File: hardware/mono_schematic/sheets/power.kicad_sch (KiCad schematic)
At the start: 37 parts

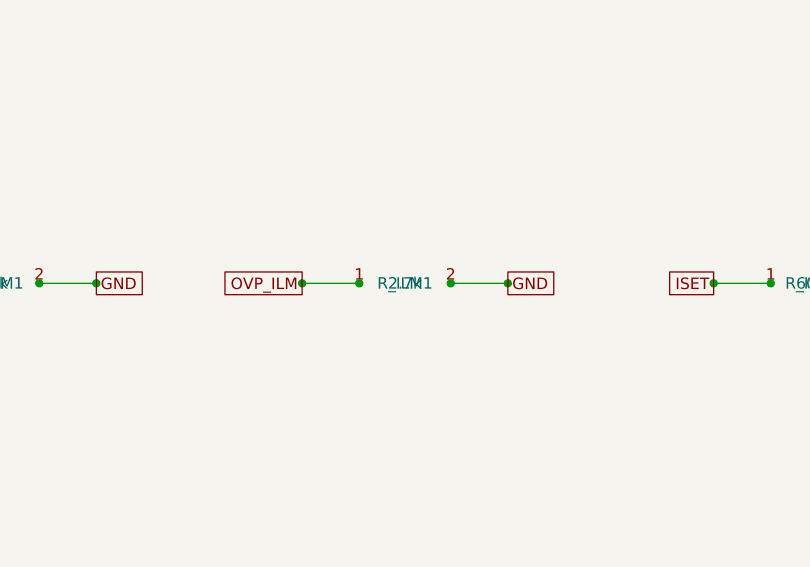
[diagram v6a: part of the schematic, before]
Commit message: mono_electronics v13c: R_ILM1 2.7k->1.6k (C4908; TPS2595 Eq.4 ILIM=2000/R+0.04 = 1.29 A, 1.19-1.39 A); U_OVP1 F GND pour 21.5 mm2 + 2 thermal vias; gates clean (DRC 0/0/0, ERC 0, 0 diffs, прозвонка 243/243); BOM/fab regen; abs-max review updated
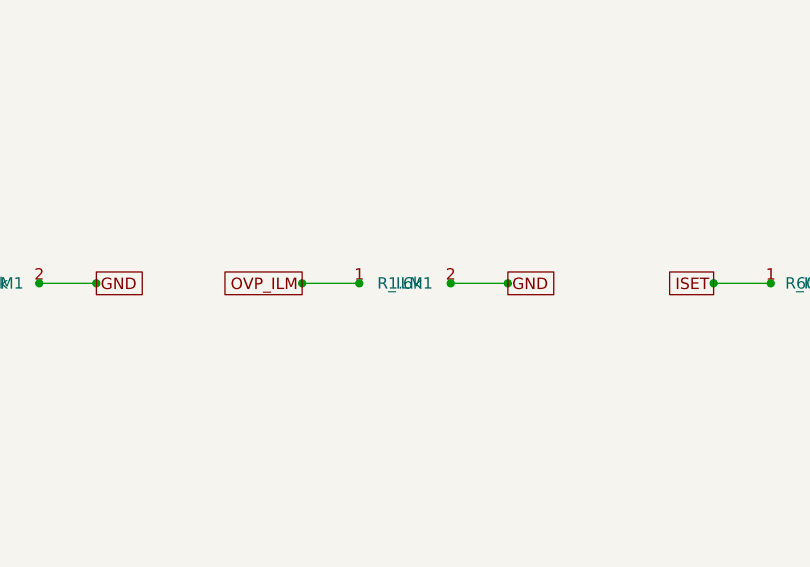
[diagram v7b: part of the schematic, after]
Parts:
- removed R_ILM1: 2.7k, mono_electronics:R_0402_1005Metric, symbol mono_parts:2.7k_R_0402_1005Metric_2
- added R_ILM1: 1.6k, mono_electronics:R_0402_1005Metric, symbol mono_parts:1.6k_R_0402_1005Metric_2
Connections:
- net GND: now also R_ILM1.2
- net OVP_ILM: now also R_ILM1.1
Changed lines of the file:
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@@
     (instances
       (project "mono_electronics"
-        (path "/706eb51d-2e2a-47df-978e-c1eb7edb736e"
+        (path "/4534f897-2767-49e5-adb1-4ac162ec0a5d"
           (reference "C_ASW_IN1")
           (unit 1)
@@
     (instances
       (project "mono_electronics"
-        (path "/706eb51d-2e2a-47df-978e-c1eb7edb736e"
+        (path "/4534f897-2767-49e5-adb1-4ac162ec0a5d"
           (reference "C_AUD_SW1")
           (unit 1)
@@
     (instances
       (project "mono_electronics"
-        (path "/706eb51d-2e2a-47df-978e-c1eb7edb736e"
+        (path "/4534f897-2767-49e5-adb1-4ac162ec0a5d"
           (reference "C_CHG_BAT1")
           (unit 1)
@@
     (instances
       (project "mono_electronics"
-        (path "/706eb51d-2e2a-47df-978e-c1eb7edb736e"
+        (path "/4534f897-2767-49e5-adb1-4ac162ec0a5d"
           (reference "C_CHG_IN1")
           (unit 1)
@@
     (instances
       (project "mono_electronics"
-        (path "/706eb51d-2e2a-47df-978e-c1eb7edb736e"
+        (path "/4534f897-2767-49e5-adb1-4ac162ec0a5d"
           (reference "C_CHG_SYS1")
           (unit 1)
@@
     (instances
       (project "mono_electronics"
-        (path "/706eb51d-2e2a-47df-978e-c1eb7edb736e"
+        (path "/4534f897-2767-49e5-adb1-4ac162ec0a5d"
           (reference "C_EN1")
           (unit 1)
@@
     (instances
       (project "mono_electronics"
-        (path "/706eb51d-2e2a-47df-978e-c1eb7edb736e"
+        (path "/4534f897-2767-49e5-adb1-4ac162ec0a5d"
           (reference "C_GAUGE1")
           (unit 1)
@@
     (instances
       (project "mono_electronics"
-        (path "/706eb51d-2e2a-47df-978e-c1eb7edb736e"
+        (path "/4534f897-2767-49e5-adb1-4ac162ec0a5d"
           (reference "C_LDO_IN1")
           (unit 1)
@@
     (instances
       (project "mono_electronics"
-        (path "/706eb51d-2e2a-47df-978e-c1eb7edb736e"
+        (path "/4534f897-2767-49e5-adb1-4ac162ec0a5d"
           (reference "C_LDO_OUT1")
           (unit 1)
@@
     (instances
       (project "mono_electronics"
-        (path "/706eb51d-2e2a-47df-978e-c1eb7edb736e"
+        (path "/4534f897-2767-49e5-adb1-4ac162ec0a5d"
           (reference "C_LED1")
           (unit 1)
@@
     (instances
       (project "mono_electronics"
-        (path "/706eb51d-2e2a-47df-978e-c1eb7edb736e"
+        (path "/4534f897-2767-49e5-adb1-4ac162ec0a5d"
           (reference "C_LED2")
           (unit 1)
@@
     (instances
       (project "mono_electronics"
-        (path "/706eb51d-2e2a-47df-978e-c1eb7edb736e"
+        (path "/4534f897-2767-49e5-adb1-4ac162ec0a5d"
           (reference "C_LL1")
           (unit 1)
@@
     (instances
       (project "mono_electronics"
-        (path "/706eb51d-2e2a-47df-978e-c1eb7edb736e"
+        (path "/4534f897-2767-49e5-adb1-4ac162ec0a5d"
           (reference "C_LL2")
           (unit 1)
@@
     (instances
       (project "mono_electronics"
-        (path "/706eb51d-2e2a-47df-978e-c1eb7edb736e"
+        (path "/4534f897-2767-49e5-adb1-4ac162ec0a5d"
           (reference "C_LL_IN1")
           (unit 1)
@@
     (instances
       (project "mono_electronics"
-        (path "/706eb51d-2e2a-47df-978e-c1eb7edb736e"
+        (path "/4534f897-2767-49e5-adb1-4ac162ec0a5d"
           (reference "C_SYS1")
           (unit 1)
@@
     (instances
       (project "mono_electronics"
-        (path "/706eb51d-2e2a-47df-978e-c1eb7edb736e"
+        (path "/4534f897-2767-49e5-adb1-4ac162ec0a5d"
           (reference "D_VBUS1")
           (unit 1)
@@
     (instances
       (project "mono_electronics"
-        (path "/706eb51d-2e2a-47df-978e-c1eb7edb736e"
+        (path "/4534f897-2767-49e5-adb1-4ac162ec0a5d"
           (reference "F_BAT1")
           (unit 1)
@@
     (instances
       (project "mono_electronics"
-        (path "/706eb51d-2e2a-47df-978e-c1eb7edb736e"
+        (path "/4534f897-2767-49e5-adb1-4ac162ec0a5d"
           (reference "J_BAT1")
           (unit 1)
@@
     (instances
       (project "mono_electronics"
-        (path "/706eb51d-2e2a-47df-978e-c1eb7edb736e"
+        (path "/4534f897-2767-49e5-adb1-4ac162ec0a5d"
           (reference "L_LED1")
           (unit 1)
@@
     (instances
       (project "mono_electronics"
-        (path "/706eb51d-2e2a-47df-978e-c1eb7edb736e"
+        (path "/4534f897-2767-49e5-adb1-4ac162ec0a5d"
           (reference "Q_BAT1")
           (unit 1)
@@
     (instances
       (project "mono_electronics"
-        (path "/706eb51d-2e2a-47df-978e-c1eb7edb736e"
+        (path "/4534f897-2767-49e5-adb1-4ac162ec0a5d"
           (reference "R_ALRT1")
           (unit 1)
@@
     (instances
       (project "mono_electronics"
-        (path "/706eb51d-2e2a-47df-978e-c1eb7edb736e"
+        (path "/4534f897-2767-49e5-adb1-4ac162ec0a5d"
           (reference "R_AUD_PD1")
           (unit 1)
@@
     (instances
       (project "mono_electronics"
-        (path "/706eb51d-2e2a-47df-978e-c1eb7edb736e"
+        (path "/4534f897-2767-49e5-adb1-4ac162ec0a5d"
           (reference "R_BATG1")
           (unit 1)
@@
     (instances
       (project "mono_electronics"
-        (path "/706eb51d-2e2a-47df-978e-c1eb7edb736e"
+        (path "/4534f897-2767-49e5-adb1-4ac162ec0a5d"
           (reference "R_FB_BOT1")
           (unit 1)
@@
     (instances
       (project "mono_electronics"
-        (path "/706eb51d-2e2a-47df-978e-c1eb7edb736e"
+        (path "/4534f897-2767-49e5-adb1-4ac162ec0a5d"
           (reference "R_FB_TOP1")
           (unit 1)
@@
     (instances
       (project "mono_electronics"
-        (path "/706eb51d-2e2a-47df-978e-c1eb7edb736e"
+        (path "/4534f897-2767-49e5-adb1-4ac162ec0a5d"
           (reference "R_ILIM1")
           (unit 1)
@@
   )
   (symbol
-    (lib_id "mono_parts:2.7k_R_0402_1005Metric_2")
+    (lib_id "mono_parts:1.6k_R_0402_1005Metric_2")
     (at 127 370.84 0)
     (unit 1)
@@
     (property
       "Value"
-      "2.7k"
+      "1.6k"
       (at 127 370.84 0)
       (effects
@@
     (instances
       (project "mono_electronics"
-        (path "/706eb51d-2e2a-47df-978e-c1eb7edb736e"
+        (path "/4534f897-2767-49e5-adb1-4ac162ec0a5d"
           (reference "R_ILM1")
           (unit 1)
@@
     (instances
       (project "mono_electronics"
-        (path "/706eb51d-2e2a-47df-978e-c1eb7edb736e"
+        (path "/4534f897-2767-49e5-adb1-4ac162ec0a5d"
           (reference "R_ISET1")
           (unit 1)
@@
     (instances
       (project "mono_electronics"
-        (path "/706eb51d-2e2a-47df-978e-c1eb7edb736e"
+        (path "/4534f897-2767-49e5-adb1-4ac162ec0a5d"
           (reference "R_LOGIC_PD1")
           (unit 1)
@@
     (instances
       (project "mono_electronics"
-        (path "/706eb51d-2e2a-47df-978e-c1eb7edb736e"
+        (path "/4534f897-2767-49e5-adb1-4ac162ec0a5d"
           (reference "R_QOD1")
           (unit 1)
@@
     (instances
       (project "mono_electronics"
-        (path "/706eb51d-2e2a-47df-978e-c1eb7edb736e"
+        (path "/4534f897-2767-49e5-adb1-4ac162ec0a5d"
           (reference "R_TH1")
           (unit 1)
@@
     (instances
       (project "mono_electronics"
-        (path "/706eb51d-2e2a-47df-978e-c1eb7edb736e"
+        (path "/4534f897-2767-49e5-adb1-4ac162ec0a5d"
           (reference "TH_PCB1")
           (unit 1)
@@
     (instances
       (project "mono_electronics"
-        (path "/706eb51d-2e2a-47df-978e-c1eb7edb736e"
+        (path "/4534f897-2767-49e5-adb1-4ac162ec0a5d"
           (reference "U_AUDIO_SW1")
           (unit 1)
@@
     (instances
       (project "mono_electronics"
-        (path "/706eb51d-2e2a-47df-978e-c1eb7edb736e"
+        (path "/4534f897-2767-49e5-adb1-4ac162ec0a5d"
           (reference "U_CHG1")
           (unit 1)
@@
     (instances
       (project "mono_electronics"
-        (path "/706eb51d-2e2a-47df-978e-c1eb7edb736e"
+        (path "/4534f897-2767-49e5-adb1-4ac162ec0a5d"
           (reference "U_GAUGE1")
           (unit 1)
@@
     (instances
       (project "mono_electronics"
-        (path "/706eb51d-2e2a-47df-978e-c1eb7edb736e"
+        (path "/4534f897-2767-49e5-adb1-4ac162ec0a5d"
           (reference "U_LDO1")
           (unit 1)
@@
     (instances
       (project "mono_electronics"
-        (path "/706eb51d-2e2a-47df-978e-c1eb7edb736e"
+        (path "/4534f897-2767-49e5-adb1-4ac162ec0a5d"
           (reference "U_OVP1")
           (unit 1)
@@
   )
   (sheet_instances
-    (path "/706eb51d-2e2a-47df-978e-c1eb7edb736e"
+    (path "/4534f897-2767-49e5-adb1-4ac162ec0a5d"
       (page "1")
     )

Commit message: mono_electronics v13d: revert R_ILM1 to 2.7k (C25885, 0.78 A eFuse limit < BQ25185 1.1 A abs max); keep U_OVP1 thermal copper/vias; abs-max note reverted; gates clean; BOM/fab regen
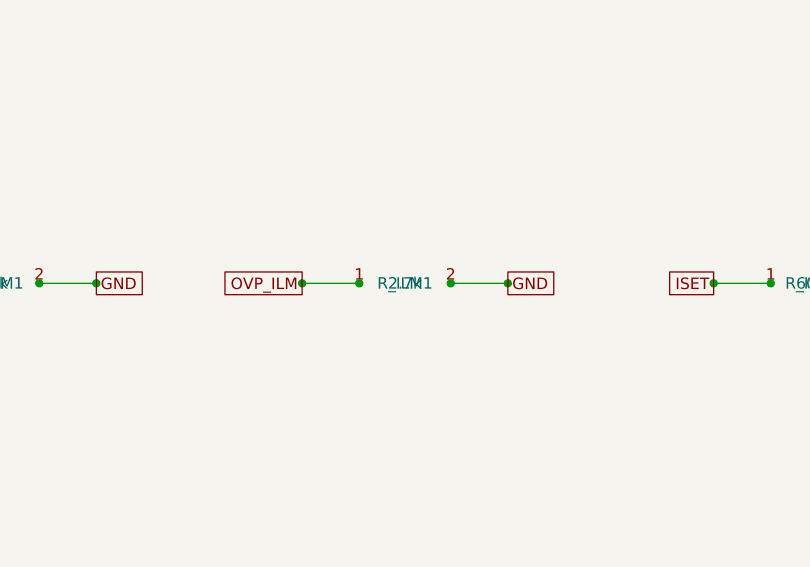
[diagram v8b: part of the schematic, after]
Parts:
- removed R_ILM1: 1.6k, mono_electronics:R_0402_1005Metric, symbol mono_parts:1.6k_R_0402_1005Metric_2
- added R_ILM1: 2.7k, mono_electronics:R_0402_1005Metric, symbol mono_parts:2.7k_R_0402_1005Metric_2
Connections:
- net GND: now also R_ILM1.2
- net OVP_ILM: now also R_ILM1.1
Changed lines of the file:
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@@
     (instances
       (project "mono_electronics"
-        (path "/4534f897-2767-49e5-adb1-4ac162ec0a5d"
+        (path "/5bbb86c3-7535-44e1-8270-8b8412fa0c37"
           (reference "C_ASW_IN1")
           (unit 1)
@@
     (instances
       (project "mono_electronics"
-        (path "/4534f897-2767-49e5-adb1-4ac162ec0a5d"
+        (path "/5bbb86c3-7535-44e1-8270-8b8412fa0c37"
           (reference "C_AUD_SW1")
           (unit 1)
@@
     (instances
       (project "mono_electronics"
-        (path "/4534f897-2767-49e5-adb1-4ac162ec0a5d"
+        (path "/5bbb86c3-7535-44e1-8270-8b8412fa0c37"
           (reference "C_CHG_BAT1")
           (unit 1)
@@
     (instances
       (project "mono_electronics"
-        (path "/4534f897-2767-49e5-adb1-4ac162ec0a5d"
+        (path "/5bbb86c3-7535-44e1-8270-8b8412fa0c37"
           (reference "C_CHG_IN1")
           (unit 1)
@@
     (instances
       (project "mono_electronics"
-        (path "/4534f897-2767-49e5-adb1-4ac162ec0a5d"
+        (path "/5bbb86c3-7535-44e1-8270-8b8412fa0c37"
           (reference "C_CHG_SYS1")
           (unit 1)
@@
     (instances
       (project "mono_electronics"
-        (path "/4534f897-2767-49e5-adb1-4ac162ec0a5d"
+        (path "/5bbb86c3-7535-44e1-8270-8b8412fa0c37"
           (reference "C_EN1")
           (unit 1)
@@
     (instances
       (project "mono_electronics"
-        (path "/4534f897-2767-49e5-adb1-4ac162ec0a5d"
+        (path "/5bbb86c3-7535-44e1-8270-8b8412fa0c37"
           (reference "C_GAUGE1")
           (unit 1)
@@
     (instances
       (project "mono_electronics"
-        (path "/4534f897-2767-49e5-adb1-4ac162ec0a5d"
+        (path "/5bbb86c3-7535-44e1-8270-8b8412fa0c37"
           (reference "C_LDO_IN1")
           (unit 1)
@@
     (instances
       (project "mono_electronics"
-        (path "/4534f897-2767-49e5-adb1-4ac162ec0a5d"
+        (path "/5bbb86c3-7535-44e1-8270-8b8412fa0c37"
           (reference "C_LDO_OUT1")
           (unit 1)
@@
     (instances
       (project "mono_electronics"
-        (path "/4534f897-2767-49e5-adb1-4ac162ec0a5d"
+        (path "/5bbb86c3-7535-44e1-8270-8b8412fa0c37"
           (reference "C_LED1")
           (unit 1)
@@
     (instances
       (project "mono_electronics"
-        (path "/4534f897-2767-49e5-adb1-4ac162ec0a5d"
+        (path "/5bbb86c3-7535-44e1-8270-8b8412fa0c37"
           (reference "C_LED2")
           (unit 1)
@@
     (instances
       (project "mono_electronics"
-        (path "/4534f897-2767-49e5-adb1-4ac162ec0a5d"
+        (path "/5bbb86c3-7535-44e1-8270-8b8412fa0c37"
           (reference "C_LL1")
           (unit 1)
@@
     (instances
       (project "mono_electronics"
-        (path "/4534f897-2767-49e5-adb1-4ac162ec0a5d"
+        (path "/5bbb86c3-7535-44e1-8270-8b8412fa0c37"
           (reference "C_LL2")
           (unit 1)
@@
     (instances
       (project "mono_electronics"
-        (path "/4534f897-2767-49e5-adb1-4ac162ec0a5d"
+        (path "/5bbb86c3-7535-44e1-8270-8b8412fa0c37"
           (reference "C_LL_IN1")
           (unit 1)
@@
     (instances
       (project "mono_electronics"
-        (path "/4534f897-2767-49e5-adb1-4ac162ec0a5d"
+        (path "/5bbb86c3-7535-44e1-8270-8b8412fa0c37"
           (reference "C_SYS1")
           (unit 1)
@@
     (instances
       (project "mono_electronics"
-        (path "/4534f897-2767-49e5-adb1-4ac162ec0a5d"
+        (path "/5bbb86c3-7535-44e1-8270-8b8412fa0c37"
           (reference "D_VBUS1")
           (unit 1)
@@
     (instances
       (project "mono_electronics"
-        (path "/4534f897-2767-49e5-adb1-4ac162ec0a5d"
+        (path "/5bbb86c3-7535-44e1-8270-8b8412fa0c37"
           (reference "F_BAT1")
           (unit 1)
@@
     (instances
       (project "mono_electronics"
-        (path "/4534f897-2767-49e5-adb1-4ac162ec0a5d"
+        (path "/5bbb86c3-7535-44e1-8270-8b8412fa0c37"
           (reference "J_BAT1")
           (unit 1)
@@
     (instances
       (project "mono_electronics"
-        (path "/4534f897-2767-49e5-adb1-4ac162ec0a5d"
+        (path "/5bbb86c3-7535-44e1-8270-8b8412fa0c37"
           (reference "L_LED1")
           (unit 1)
@@
     (instances
       (project "mono_electronics"
-        (path "/4534f897-2767-49e5-adb1-4ac162ec0a5d"
+        (path "/5bbb86c3-7535-44e1-8270-8b8412fa0c37"
           (reference "Q_BAT1")
           (unit 1)
@@
     (instances
       (project "mono_electronics"
-        (path "/4534f897-2767-49e5-adb1-4ac162ec0a5d"
+        (path "/5bbb86c3-7535-44e1-8270-8b8412fa0c37"
           (reference "R_ALRT1")
           (unit 1)
@@
     (instances
       (project "mono_electronics"
-        (path "/4534f897-2767-49e5-adb1-4ac162ec0a5d"
+        (path "/5bbb86c3-7535-44e1-8270-8b8412fa0c37"
           (reference "R_AUD_PD1")
           (unit 1)
@@
     (instances
       (project "mono_electronics"
-        (path "/4534f897-2767-49e5-adb1-4ac162ec0a5d"
+        (path "/5bbb86c3-7535-44e1-8270-8b8412fa0c37"
           (reference "R_BATG1")
           (unit 1)
@@
     (instances
       (project "mono_electronics"
-        (path "/4534f897-2767-49e5-adb1-4ac162ec0a5d"
+        (path "/5bbb86c3-7535-44e1-8270-8b8412fa0c37"
           (reference "R_FB_BOT1")
           (unit 1)
@@
     (instances
       (project "mono_electronics"
-        (path "/4534f897-2767-49e5-adb1-4ac162ec0a5d"
+        (path "/5bbb86c3-7535-44e1-8270-8b8412fa0c37"
           (reference "R_FB_TOP1")
           (unit 1)
@@
     (instances
       (project "mono_electronics"
-        (path "/4534f897-2767-49e5-adb1-4ac162ec0a5d"
+        (path "/5bbb86c3-7535-44e1-8270-8b8412fa0c37"
           (reference "R_ILIM1")
           (unit 1)
@@
   )
   (symbol
-    (lib_id "mono_parts:1.6k_R_0402_1005Metric_2")
+    (lib_id "mono_parts:2.7k_R_0402_1005Metric_2")
     (at 127 370.84 0)
     (unit 1)
@@
     (property
       "Value"
-      "1.6k"
+      "2.7k"
       (at 127 370.84 0)
       (effects
@@
     (instances
       (project "mono_electronics"
-        (path "/4534f897-2767-49e5-adb1-4ac162ec0a5d"
+        (path "/5bbb86c3-7535-44e1-8270-8b8412fa0c37"
           (reference "R_ILM1")
           (unit 1)
@@
     (instances
       (project "mono_electronics"
-        (path "/4534f897-2767-49e5-adb1-4ac162ec0a5d"
+        (path "/5bbb86c3-7535-44e1-8270-8b8412fa0c37"
           (reference "R_ISET1")
           (unit 1)
@@
     (instances
       (project "mono_electronics"
-        (path "/4534f897-2767-49e5-adb1-4ac162ec0a5d"
+        (path "/5bbb86c3-7535-44e1-8270-8b8412fa0c37"
           (reference "R_LOGIC_PD1")
           (unit 1)
@@
     (instances
       (project "mono_electronics"
-        (path "/4534f897-2767-49e5-adb1-4ac162ec0a5d"
+        (path "/5bbb86c3-7535-44e1-8270-8b8412fa0c37"
           (reference "R_QOD1")
           (unit 1)
@@
     (instances
       (project "mono_electronics"
-        (path "/4534f897-2767-49e5-adb1-4ac162ec0a5d"
+        (path "/5bbb86c3-7535-44e1-8270-8b8412fa0c37"
           (reference "R_TH1")
           (unit 1)
@@
     (instances
       (project "mono_electronics"
-        (path "/4534f897-2767-49e5-adb1-4ac162ec0a5d"
+        (path "/5bbb86c3-7535-44e1-8270-8b8412fa0c37"
           (reference "TH_PCB1")
           (unit 1)
@@
     (instances
       (project "mono_electronics"
-        (path "/4534f897-2767-49e5-adb1-4ac162ec0a5d"
+        (path "/5bbb86c3-7535-44e1-8270-8b8412fa0c37"
           (reference "U_AUDIO_SW1")
           (unit 1)
@@
     (instances
       (project "mono_electronics"
-        (path "/4534f897-2767-49e5-adb1-4ac162ec0a5d"
+        (path "/5bbb86c3-7535-44e1-8270-8b8412fa0c37"
           (reference "U_CHG1")
           (unit 1)
@@
     (instances
       (project "mono_electronics"
-        (path "/4534f897-2767-49e5-adb1-4ac162ec0a5d"
+        (path "/5bbb86c3-7535-44e1-8270-8b8412fa0c37"
           (reference "U_GAUGE1")
           (unit 1)
@@
     (instances
       (project "mono_electronics"
-        (path "/4534f897-2767-49e5-adb1-4ac162ec0a5d"
+        (path "/5bbb86c3-7535-44e1-8270-8b8412fa0c37"
           (reference "U_LDO1")
           (unit 1)
@@
     (instances
       (project "mono_electronics"
-        (path "/4534f897-2767-49e5-adb1-4ac162ec0a5d"
+        (path "/5bbb86c3-7535-44e1-8270-8b8412fa0c37"
           (reference "U_OVP1")
           (unit 1)
@@
   )
   (sheet_instances
-    (path "/4534f897-2767-49e5-adb1-4ac162ec0a5d"
+    (path "/5bbb86c3-7535-44e1-8270-8b8412fa0c37"
       (page "1")
     )
